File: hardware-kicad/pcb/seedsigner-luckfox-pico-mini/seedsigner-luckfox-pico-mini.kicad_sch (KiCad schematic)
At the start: 22 parts, among them U1 LuckFox_Pico_MINI, U2 RASPBERRY_PI_3_MODEL_B+

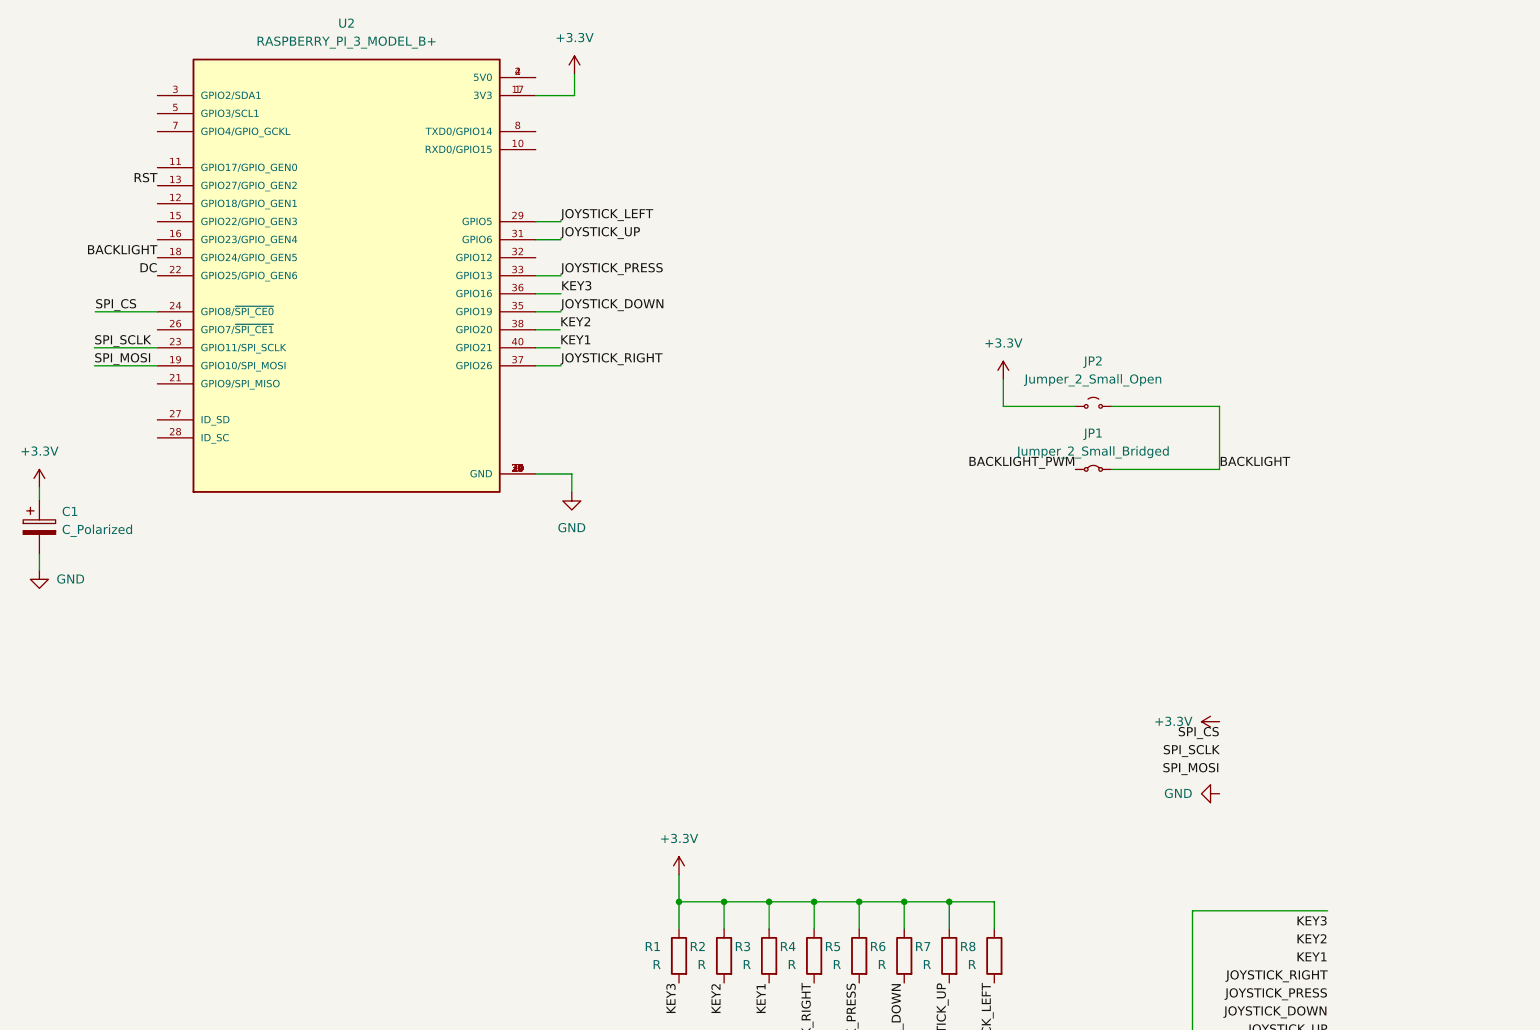
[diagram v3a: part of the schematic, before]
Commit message: cleanup project paths and make sure symbols and footprints are committed
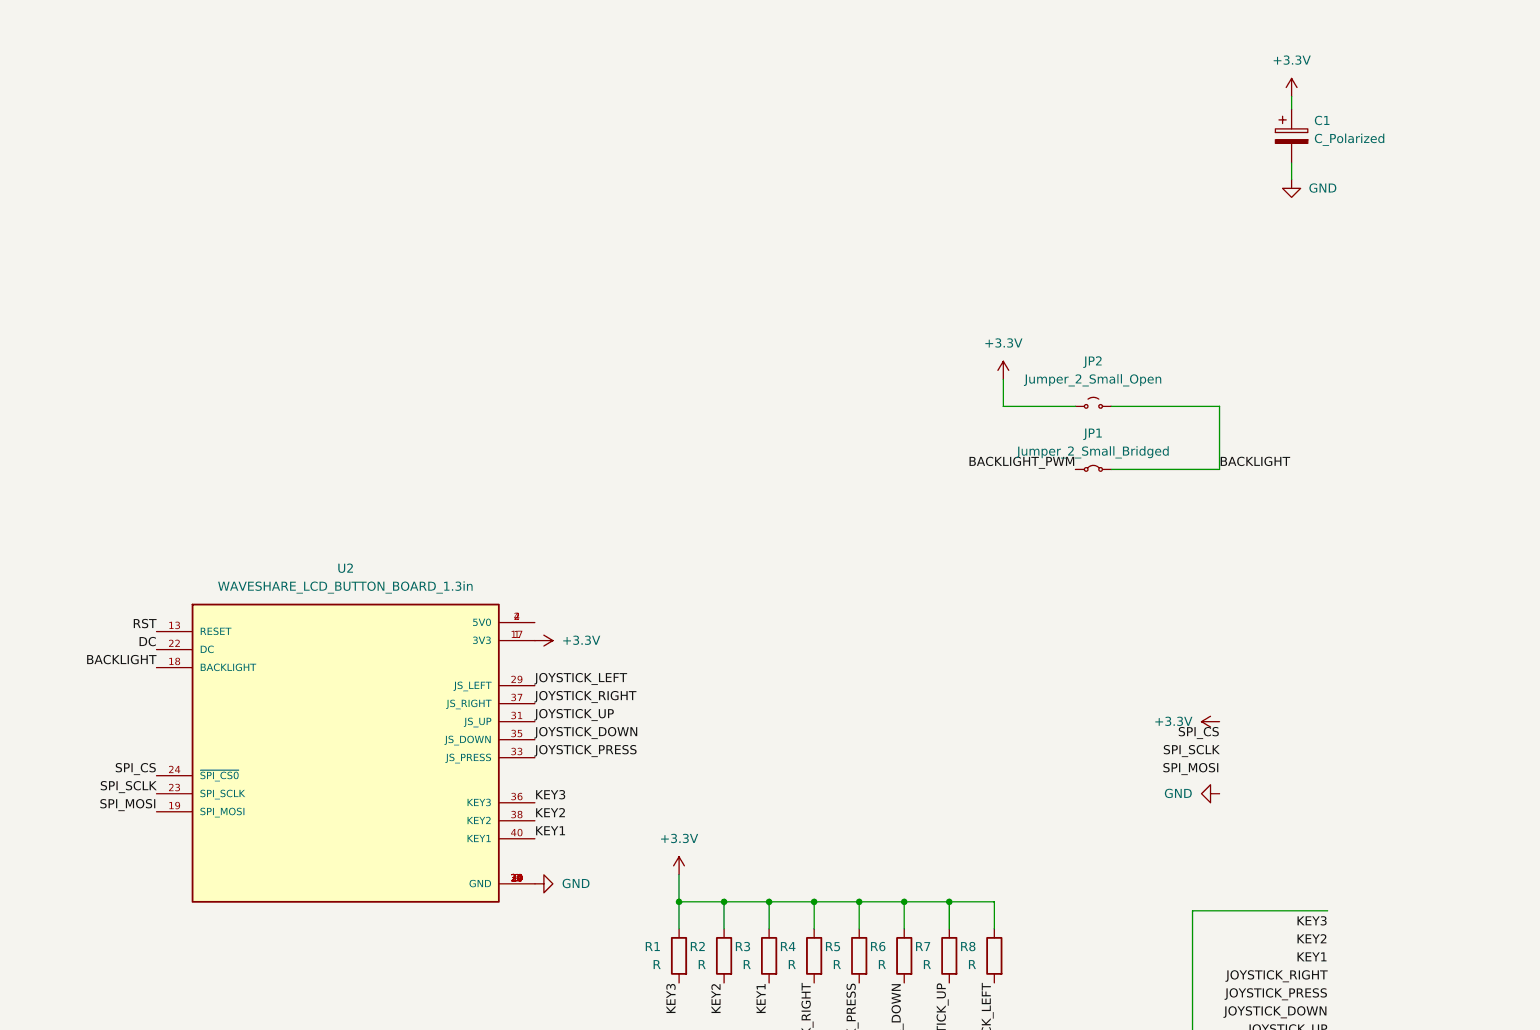
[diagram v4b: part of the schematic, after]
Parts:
- removed U2: RASPBERRY_PI_3_MODEL_B+, seedsigner-luckfox:WAVESHARE_LCD_BUTTON, symbol SeedSigner:RASPBERRY_PI_3_MODEL_B+
- added U2: WAVESHARE_LCD_BUTTON_BOARD_1.3in, seedsigner-luckfox:WAVESHARE_LCD_BUTTON, symbol SeedSigner:WAVESHARE_LCD_BUTTON
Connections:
- net +3.3V: now also U2.1 (3V3), U2.17 (3V3)
- net BACKLIGHT: now also U2.18 (BACKLIGHT)
- net DC: now also U2.22 (DC)
- net GND: now also U2.14 (GND), U2.20 (GND), U2.25 (GND), U2.30 (GND), U2.34 (GND), U2.39 (GND), U2.6 (GND), U2.9 (GND)
- net JOYSTICK_DOWN: now also U2.35 (JS_DOWN)
- net JOYSTICK_LEFT: now also U2.29 (JS_LEFT)
- net JOYSTICK_PRESS: now also U2.33 (JS_PRESS)
- net JOYSTICK_RIGHT: now also U2.37 (JS_RIGHT)
- net JOYSTICK_UP: now also U2.31 (JS_UP)
- net KEY1: now also U2.40 (KEY1)
- net KEY2: now also U2.38 (KEY2)
- net KEY3: now also U2.36 (KEY3)
- net RST: now also U2.13 (RESET)
- net SPI_CS: now also U2.24 (~{SPI_CS0})
- net SPI_MOSI: now also U2.19 (SPI_MOSI)
- net SPI_SCLK: now also U2.23 (SPI_SCLK)
- new net: U2.2 (5V0), U2.4 (5V0)
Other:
- moved on the sheet: C1
